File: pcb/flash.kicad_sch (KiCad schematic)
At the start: 4 parts, among them SW501 SW_Push, U501 W25Q128JVS

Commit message: add footprints
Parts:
- C501: footprint (none) -> Capacitor_SMD:C_1210_3225Metric_Pad1.33x2.70mm_HandSolder
- R501: footprint (none) -> Resistor_SMD:R_1210_3225Metric_Pad1.30x2.65mm_HandSolder
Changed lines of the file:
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@@
 			)
 		)
-		(property "Footprint" ""
+		(property "Footprint" "Capacitor_SMD:C_1210_3225Metric_Pad1.33x2.70mm_HandSolder"
 			(at 163.5252 85.09 0)
 			(effects
@@
 			)
 		)
-		(property "Footprint" ""
+		(property "Footprint" "Resistor_SMD:R_1210_3225Metric_Pad1.30x2.65mm_HandSolder"
 			(at 130.302 87.63 90)
 			(effects

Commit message: add footprints
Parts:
- SW501: footprint (none) -> rp2040-devboard:SW_SPST_EVPBV; Distributor link (none) -> https://mou.sr/4aZdR1f
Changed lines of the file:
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@@
 			)
 		)
-		(property "Footprint" ""
+		(property "Footprint" "rp2040-devboard:SW_SPST_EVPBV"
 			(at 121.92 109.22 0)
 			(effects
@@
 			(effects
 				(font
+					(size 1.27 1.27)
+				)
+				(hide yes)
+			)
+		)
+		(property "Distributor link" "https://mou.sr/4aZdR1f"
+			(at 116.84 109.22 90)
+			(effects
+				(font

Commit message: change footprint
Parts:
- C501: footprint Capacitor_SMD:C_1210_3225Metric_Pad1.33x2.70mm_HandSolder -> Capacitor_SMD:C_0603_1608Metric_Pad1.08x0.95mm_HandSolder
- R501: footprint Resistor_SMD:R_1210_3225Metric_Pad1.30x2.65mm_HandSolder -> Resistor_SMD:R_0603_1608Metric_Pad0.98x0.95mm_HandSolder
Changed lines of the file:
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@@
 			)
 		)
-		(property "Footprint" "Capacitor_SMD:C_1210_3225Metric_Pad1.33x2.70mm_HandSolder"
+		(property "Footprint" "Capacitor_SMD:C_0603_1608Metric_Pad1.08x0.95mm_HandSolder"
 			(at 163.5252 85.09 0)
 			(effects
@@
 			)
 		)
-		(property "Footprint" "Resistor_SMD:R_1210_3225Metric_Pad1.30x2.65mm_HandSolder"
+		(property "Footprint" "Resistor_SMD:R_0603_1608Metric_Pad0.98x0.95mm_HandSolder"
 			(at 130.302 87.63 90)
 			(effects

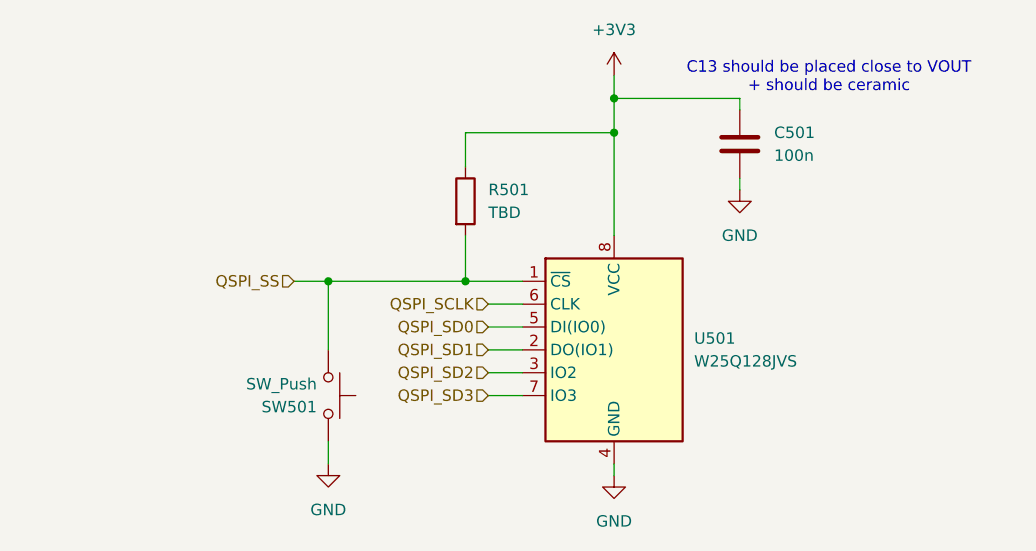
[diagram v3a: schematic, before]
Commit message: add debouncing capacitor value and dnp pull up
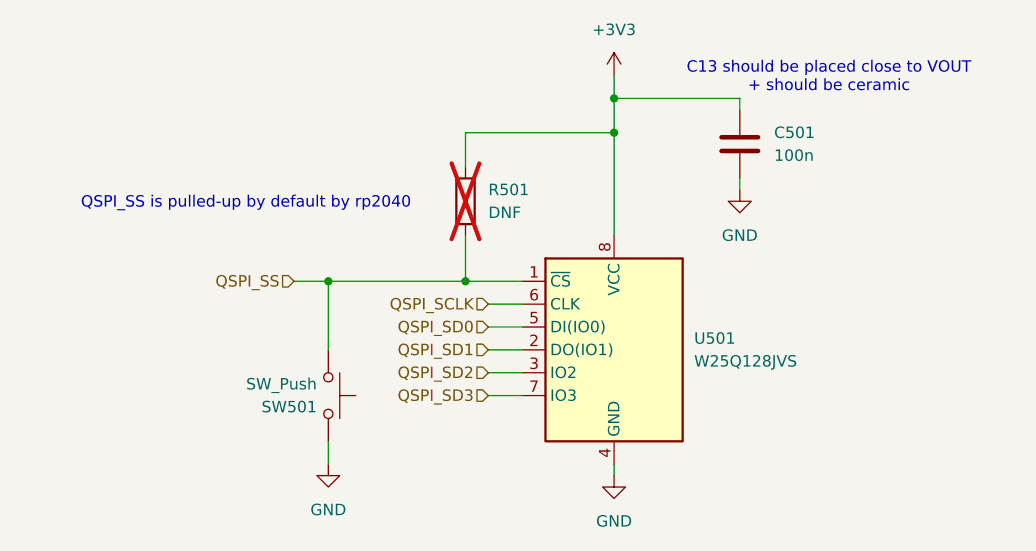
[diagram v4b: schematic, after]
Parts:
- R501: value TBD -> DNF; now not fitted
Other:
- note added: "QSPI_SS is pulled-up by default by rp2040"
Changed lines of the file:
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@@
+		)
+	)
+	(text "QSPI_SS is pulled-up by default by rp2040"
+		(exclude_from_sim no)
+		(at 107.696 87.884 0)
+		(effects
+			(font
+				(size 1.27 1.27)
+			)
 		)
 	)
@@
 		(in_bom yes)
 		(on_board yes)
-		(dnp no)
+		(dnp yes)
 		(fields_autoplaced yes)
 		(property "Reference" "R501"
@@
 			)
 		)
-		(property "Value" "TBD"
+		(property "Value" "DNF"
 			(at 134.62 88.8999 0)
 			(effects
